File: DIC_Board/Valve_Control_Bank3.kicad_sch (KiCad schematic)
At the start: 10 parts, among them U22 DRV8823QDCARQ1

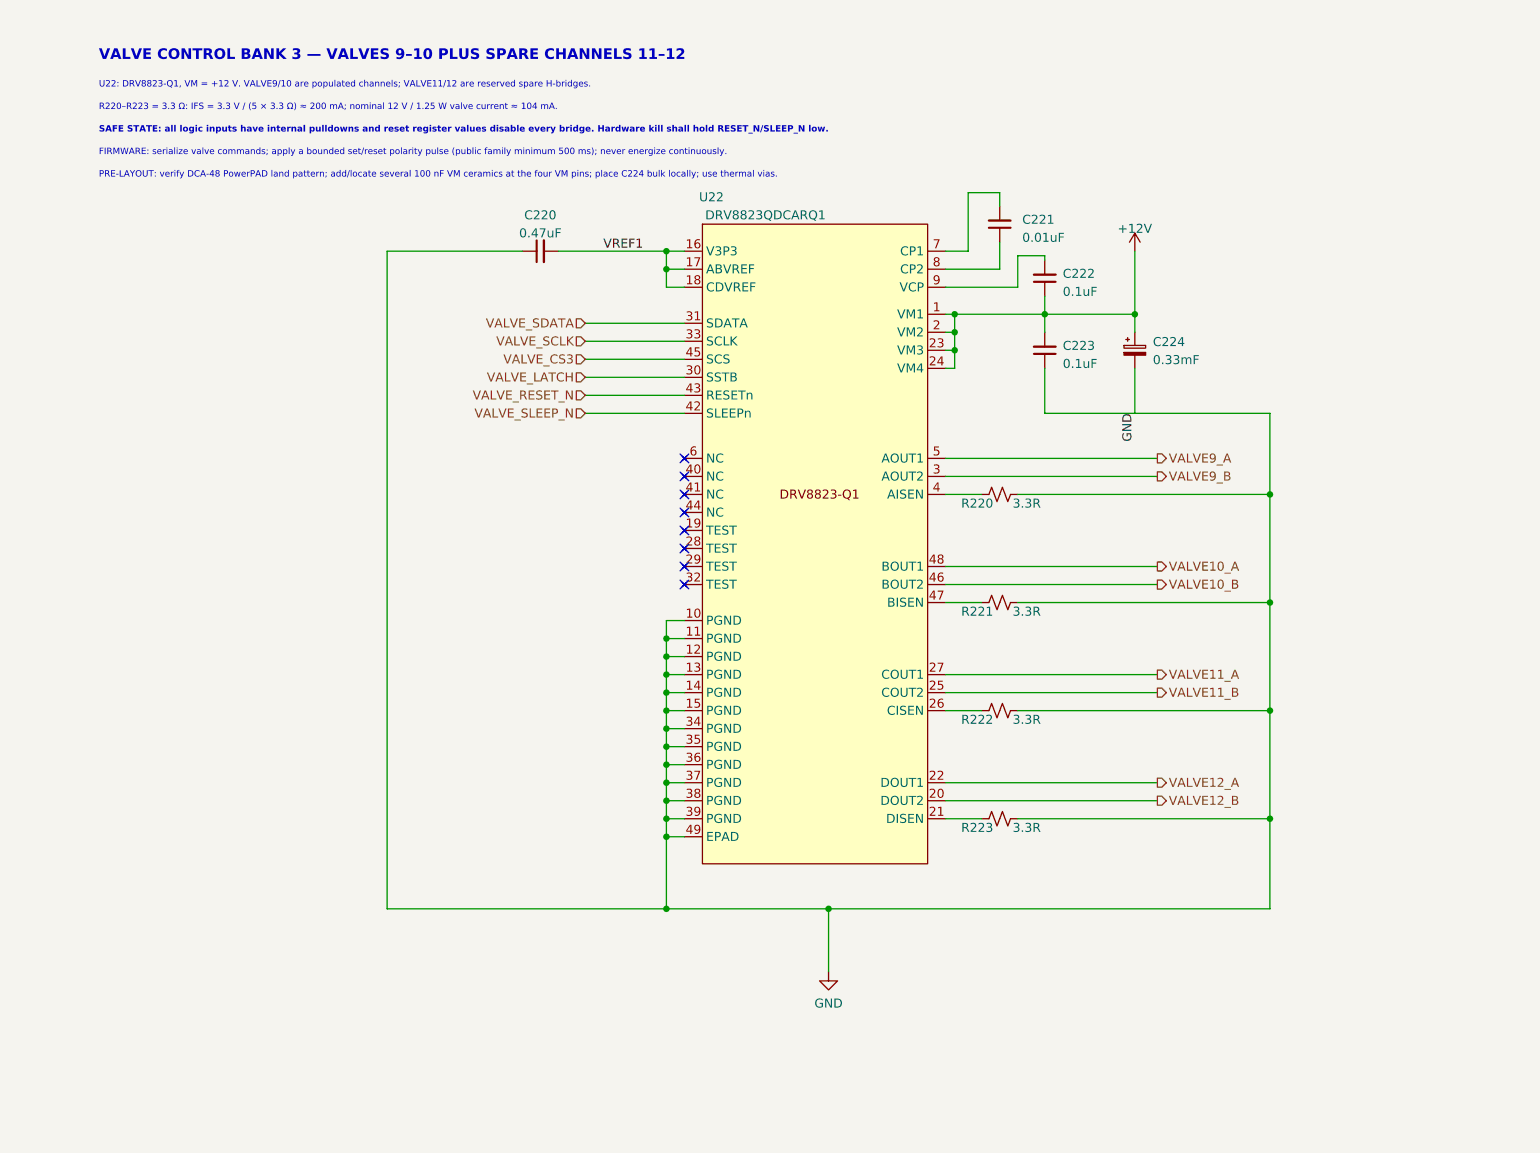
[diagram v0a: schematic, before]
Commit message: Completed water pump and added the 2.7V rail
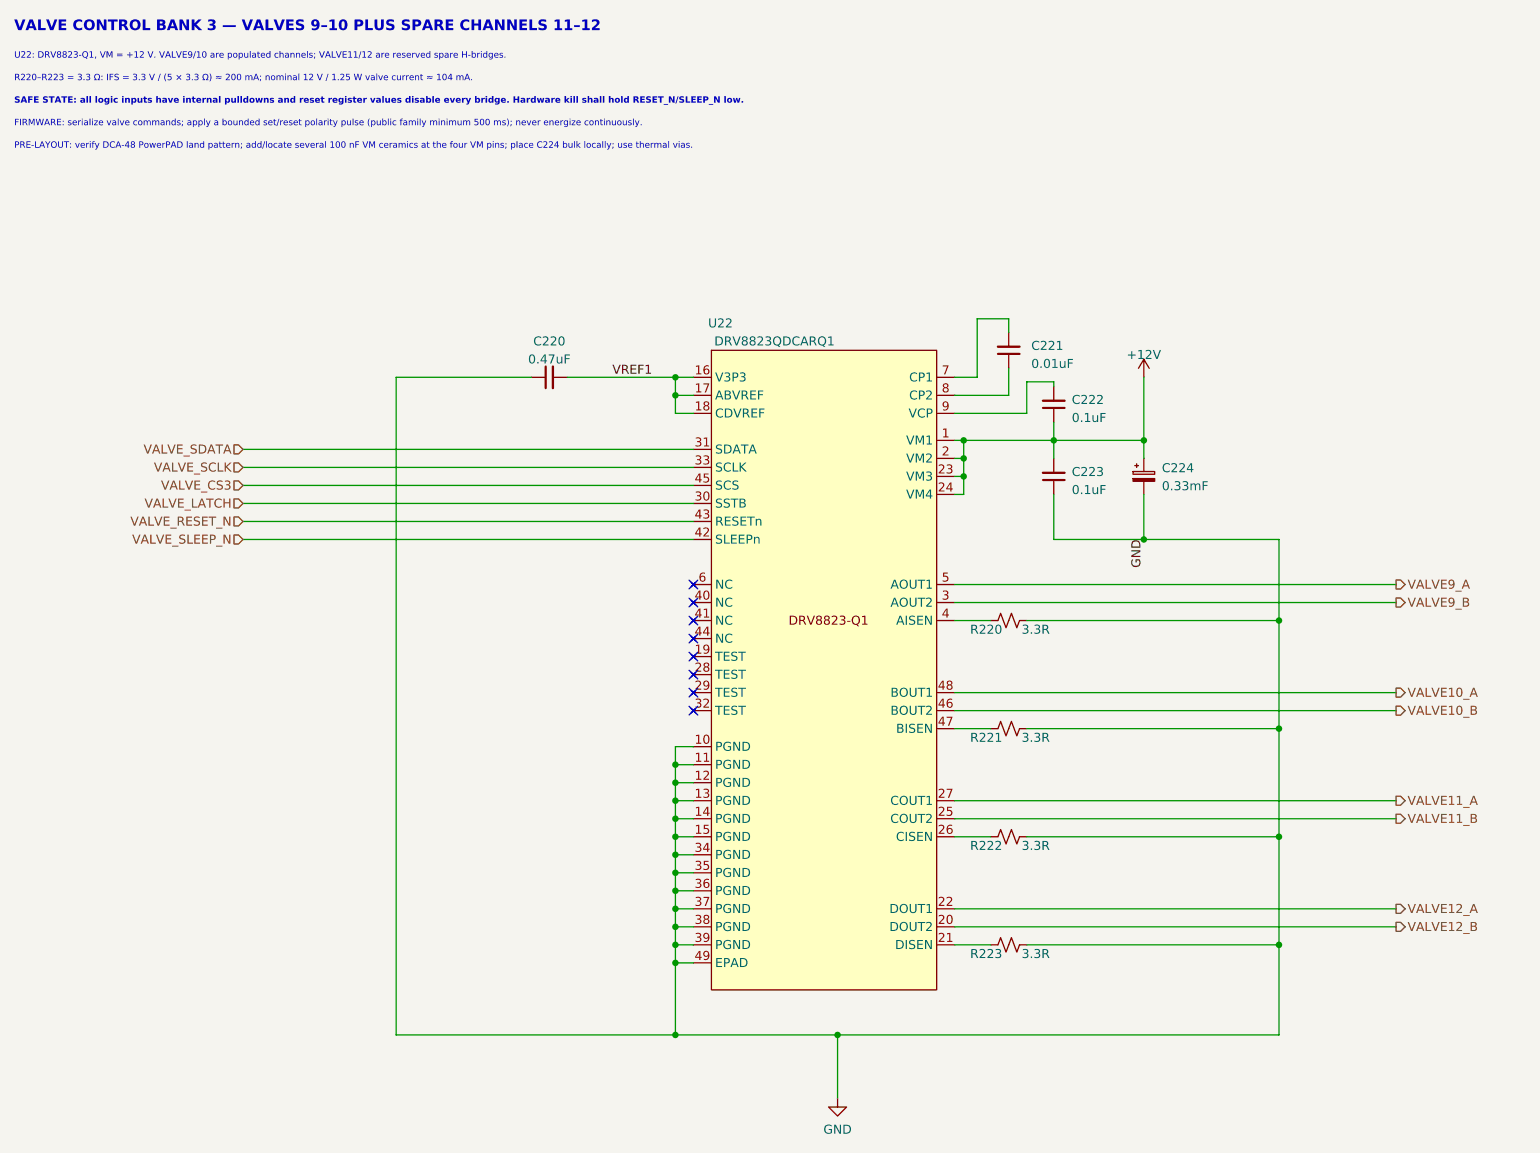
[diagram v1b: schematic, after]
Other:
- moved on the sheet: C220, C221, C222, C223, C224, R220, R221, R222, R223, U22

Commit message: Completed Acid Pump sheet
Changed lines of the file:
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@@
-		)
-	)
-	(label "GND"
-		(at 172.72 87.63 270)
-		(effects
-			(font
-				(size 1.27 1.27)
-			)
-			(justify right bottom)
 		)
 	)

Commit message: Wrapping up schematic
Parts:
- removed R220, R221, R222, R223: 3.3R, Resistor_SMD:R_1206_3216Metric, symbol Device:R_Small_US
- added R336, R337, R338, R339: 3.3R, Resistor_SMD:R_0402_1005Metric, symbol Device:R
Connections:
- net GND: now also R336.2, R337.2, R338.2, R339.2
- net at U22.26 (CISEN): now also R338.1
- net at U22.21 (DISEN): now also R339.1
- net at U22.4 (AISEN): now also R336.1
- net at U22.47 (BISEN): now also R337.1

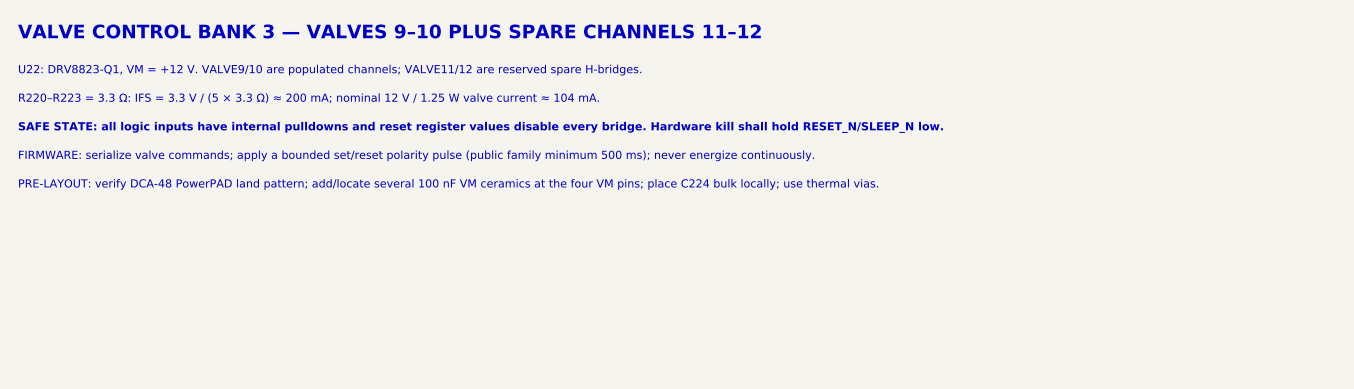
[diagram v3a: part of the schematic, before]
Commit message: Synchronize power, communications, and MCU configuration
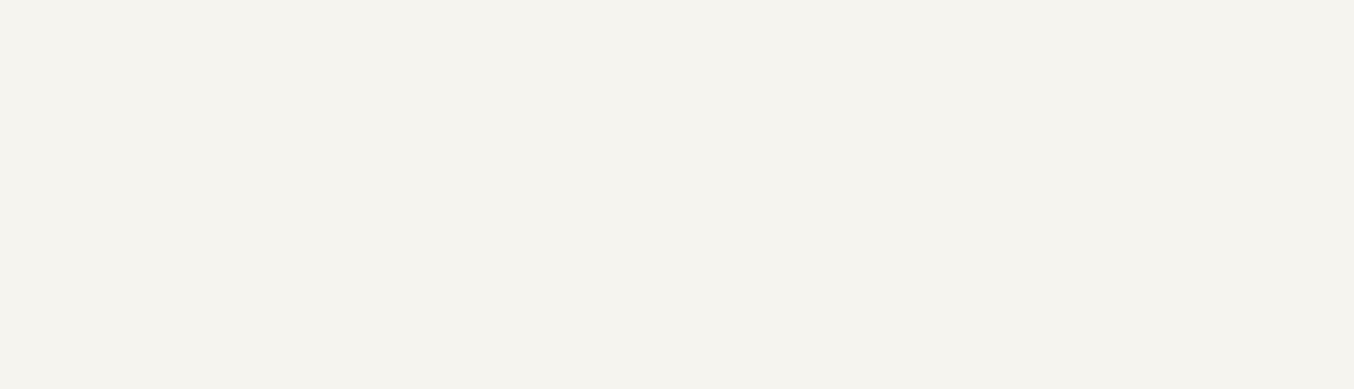
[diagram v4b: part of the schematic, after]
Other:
- note removed: "FIRMWARE: serialize valve commands; apply a bounded set/reset polarity pulse (public family minimum 500 ms); never energize continuously."
- note removed: "PRE-LAYOUT: verify DCA-48 PowerPAD land pattern; add/locate several 100 nF VM ceramics at the four VM pins; place C224 bulk locally; use thermal vias."
- note removed: "R220–R223 = 3.3 Ω: IFS = 3.3 V / (5 × 3.3 Ω) ≈ 200 mA; nominal 12 V / 1.25 W valve current ≈ 104 mA."
- note removed: "SAFE STATE: all logic inputs have internal pulldowns and reset register values disable every bridge. Hardware kill shall hold RESET_N/SLEEP_N low."
- note removed: "U22: DRV8823-Q1, VM = +12 V. VALVE9/10 are populated channels; VALVE11/12 are reserved spare H-bridges."
- note removed: "VALVE CONTROL BANK 3 — VALVES 9–10 PLUS SPARE CHANNELS 11–12"
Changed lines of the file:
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@@
 		(comment 2 "DRV8823-Q1 serial quad H-bridge")
-	)
-	(text "PRE-LAYOUT: verify DCA-48 PowerPAD land pattern; add/locate several 100 nF VM ceramics at the four VM pins; place C224 bulk locally; use thermal vias."
-		(exclude_from_sim no)
-		(at 13.462 32.766 0)
-		(effects
-			(font
-				(size 0.9 0.9)
-			)
-			(justify left bottom)
-		)
-	)
-	(text "FIRMWARE: serialize valve commands; apply a bounded set/reset polarity pulse (public family minimum 500 ms); never energize continuously."
-		(exclude_from_sim no)
-		(at 13.462 29.591 0)
-		(effects
-			(font
-				(size 0.9 0.9)
-			)
-			(justify left bottom)
-		)
-	)
-	(text "VALVE CONTROL BANK 3 — VALVES 9–10 PLUS SPARE CHANNELS 11–12"
-		(exclude_from_sim no)
-		(at 13.462 16.256 0)
-		(effects
-			(font
-				(size 1.5 1.5)
-				(bold yes)
-			)
-			(justify left bottom)
-		)
-	)
-	(text "U22: DRV8823-Q1, VM = +12 V. VALVE9/10 are populated channels; VALVE11/12 are reserved spare H-bridges."
-		(exclude_from_sim no)
-		(at 13.462 20.066 0)
-		(effects
-			(font
-				(size 0.9 0.9)
-			)
-			(justify left bottom)
-		)
-	)
-	(text "SAFE STATE: all logic inputs have internal pulldowns and reset register values disable every bridge. Hardware kill shall hold RESET_N/SLEEP_N low."
-		(exclude_from_sim no)
-		(at 13.462 26.416 0)
-		(effects
-			(font
-				(size 0.9 0.9)
-				(bold yes)
-			)
-			(justify left bottom)
-		)
-	)
-	(text "R220–R223 = 3.3 Ω: IFS = 3.3 V / (5 × 3.3 Ω) ≈ 200 mA; nominal 12 V / 1.25 W valve current ≈ 104 mA."
-		(exclude_from_sim no)
-		(at 13.462 23.241 0)
-		(effects
-			(font
-				(size 0.9 0.9)
-			)
-			(justify left bottom)
-		)
 	)
 	(junction

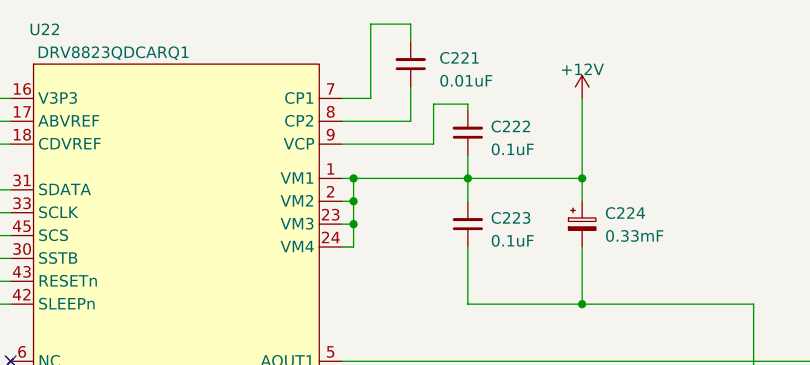
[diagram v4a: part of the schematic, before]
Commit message: Updated board for layout! All footprints added
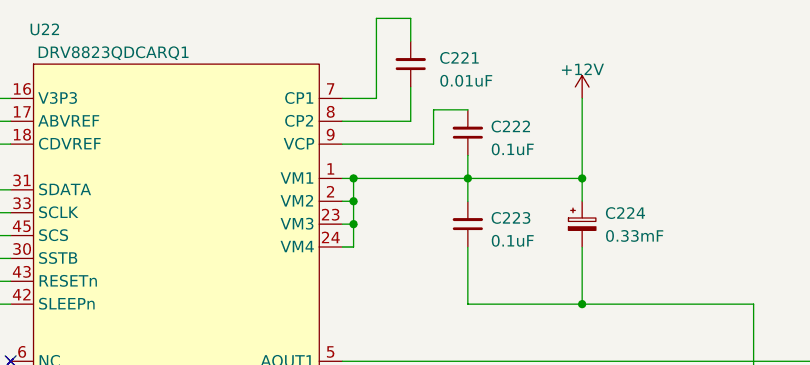
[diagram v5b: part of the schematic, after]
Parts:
- C220: Manufacturer (none) -> TDK
- C221, C222, C223: Manufacturer (none) -> KEMET
- C224: Manufacturer (none) -> Nichicon
- R336, R337, R338, R339: BOM Source (none) -> https://www.vishay.com/docs/20043/crcwhpe3.pdf; MPN (none) -> CRCW04023R30FKEDHP; Manufacturer Vishay Dale -> Vishay; Power Rating (none) -> 0.2W; Tolerance (none) -> 1%
- U22: footprint DIC_Board:HTSSOP48 -> DIC_Board:DRV8823_DCA48_ReviewFixed; Manufacturer (none) -> Texas Instruments

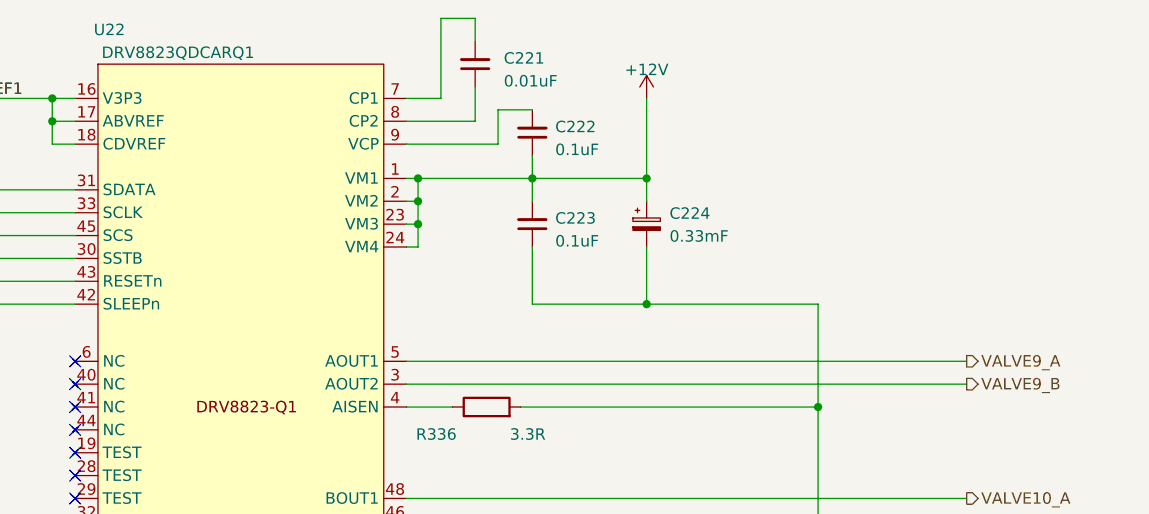
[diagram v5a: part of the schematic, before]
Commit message: Changed the 12V regulator to an integrated IC
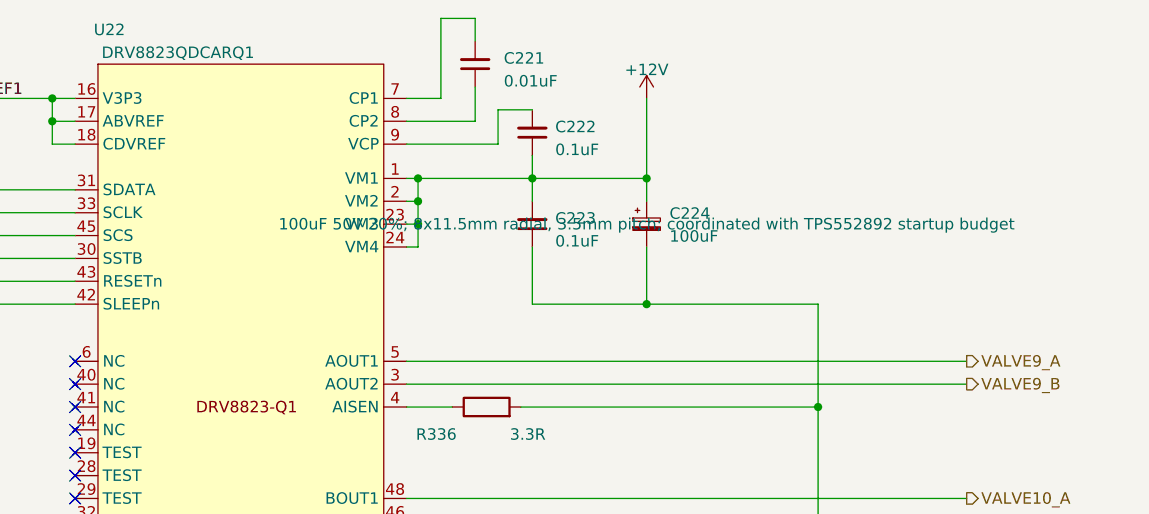
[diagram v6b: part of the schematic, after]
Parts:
- C224: value 0.33mF -> 100uF; footprint Capacitor_THT:CP_Radial_D12.5mm_P5.00mm -> Capacitor_THT:CP_Radial_D8.0mm_P3.50mm; MPN URZ1H331MHD1TO -> UHE1H101MPD
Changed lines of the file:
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@@
 			)
 		)
-		(property "Value" "0.33mF"
+		(property "Value" "100uF"
 			(at 175.26 80.0989 0)
 			(show_name no)
@@
 			)
 		)
-		(property "Footprint" "Capacitor_THT:CP_Radial_D12.5mm_P5.00mm"
+		(property "Footprint" "Capacitor_THT:CP_Radial_D8.0mm_P3.50mm"
 			(at 172.72 78.74 0)
 			(hide yes)
@@
 			)
 		)
-		(property "Datasheet" ""
+		(property "Datasheet" "https://www.nichicon.com/getmedia/5ee6e3a3-2d90-4858-bed0-89ef58a93bc3/e-uhe.pdf"
 			(at 172.72 78.74 0)
 			(hide yes)
@@
 			)
 		)
-		(property "Description" ""
+		(property "Description" "100uF 50V 20%; 8x11.5mm radial, 3.5mm pitch; coordinated with TPS552892 startup budget"
 			(at 172.72 78.74 0)
 			(show_name no)
@@
 			)
 		)
-		(property "MPN" "URZ1H331MHD1TO"
+		(property "MPN" "UHE1H101MPD"
 			(at 172.72 78.74 0)
 			(hide yes)
@@
 			(at 0 0 0)
 			(hide yes)
+			(show_name no)
+			(do_not_autoplace no)
+			(effects
+				(font
+					(size 1.27 1.27)
+				)
+			)
+		)
+		(property "Mouser" ""
+			(at 0 0 0)
+			(hide yes)
+			(show_name no)
+			(do_not_autoplace no)
+			(effects
+				(font
+					(size 1.27 1.27)
+				)
+			)
+		)
+		(property "DigiKey" ""
+			(at 0 0 0)
+			(hide yes)
